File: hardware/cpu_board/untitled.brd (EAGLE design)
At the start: 126.3 x 94.6 mm, 83 parts, among them IC1 MAX232ECWE, IC2 MAX232ECWE, IC3 AM29F040J, IC4 74HCT138D, IC5 LM2596S, IC6 74HCT273DW, IC7 74LVC1G08DBV, IC8 74LVC1G04DBV, IC9 74HCT138D, J2 POWER_JACKSLT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

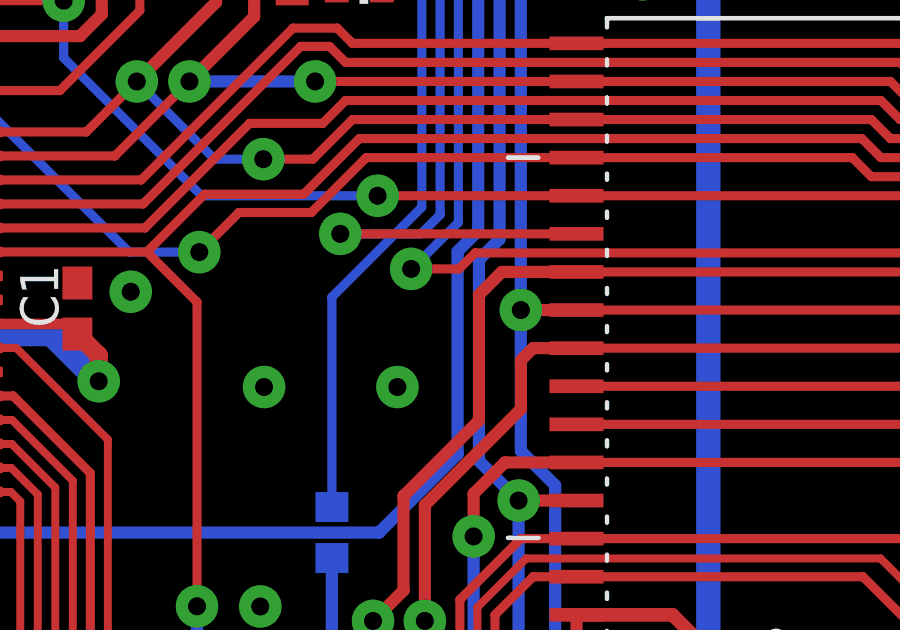
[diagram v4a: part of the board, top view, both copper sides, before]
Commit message: Mionor bug fixed
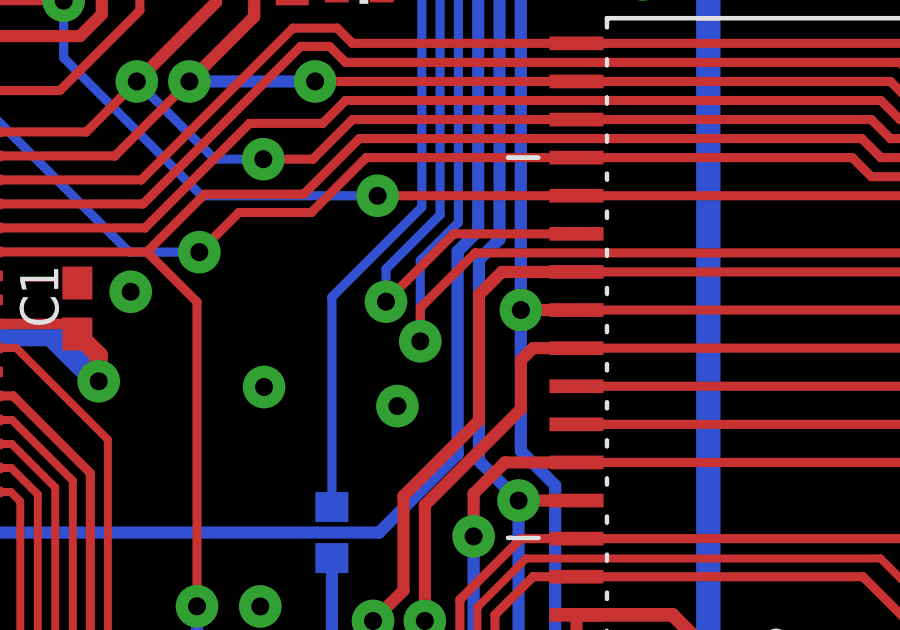
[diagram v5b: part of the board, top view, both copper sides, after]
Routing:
- net !ROM_CS: track 59.5 -> 63.2 mm
- net !RAM_CS: track 52.1 -> 51.6 mm
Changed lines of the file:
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@@
 <contactref element="IC9" pad="1"/>
 <contactref element="IC9" pad="5"/>
-<via x="67.7418" y="34.8234" extent="1-16" drill="0.6" diameter="1.4224" shape="octagon"/>
+<via x="67.7418" y="34.1884" extent="1-16" drill="0.6" diameter="1.4224" shape="octagon"/>
 <wire x1="4.064" y1="-9.359" x2="16.6624" y2="-7.9398" width="0" layer="19" extent="1-1"/>
 <wire x1="14.605" y1="7.62" x2="16.6624" y2="-7.9398" width="0" layer="19" extent="1-1"/>
@@
 <contactref element="IC3" pad="22"/>
 <wire x1="95.6206" y1="39.2938" x2="70.3326" y2="39.2938" width="0.3048" layer="1"/>
-<via x="68.199" y="38.7604" extent="1-16" drill="0.6" diameter="1.4224" shape="octagon"/>
-<wire x1="68.199" y1="38.7604" x2="69.7992" y2="38.7604" width="0.3048" layer="1"/>
-<wire x1="69.7992" y1="38.7604" x2="70.3326" y2="39.2938" width="0.3048" layer="1"/>
+<via x="68.5038" y="36.3474" extent="1-16" drill="0.6" diameter="1.4224" shape="octagon"/>
 <wire x1="65.4304" y1="54.864" x2="65.4304" y2="61.1886" width="0.3048" layer="16"/>
 <contactref element="IC9" pad="15"/>
-<wire x1="68.199" y1="38.7604" x2="68.2244" y2="38.7604" width="0.3048" layer="16"/>
-<wire x1="68.2244" y1="38.7604" x2="69.7738" y2="40.3098" width="0.3048" layer="16"/>
+<wire x1="68.5038" y1="39.0398" x2="69.7738" y2="40.3098" width="0.3048" layer="16"/>
 <wire x1="69.7738" y1="40.3098" x2="69.7738" y2="50.5206" width="0.3048" layer="16"/>
 <wire x1="61.6966" y1="66.6496" x2="61.6966" y2="64.9224" width="0.3048" layer="16"/>
 <wire x1="61.6966" y1="64.9224" x2="65.4304" y2="61.1886" width="0.3048" layer="16"/>
 <wire x1="69.7738" y1="50.5206" x2="65.4304" y2="54.864" width="0.3048" layer="16"/>
+<wire x1="68.5038" y1="36.3474" x2="68.5038" y2="39.0398" width="0.3048" layer="16"/>
+<wire x1="68.5038" y1="36.3474" x2="68.5038" y2="37.465" width="0.3048" layer="1"/>
+<wire x1="68.5038" y1="37.465" x2="70.3326" y2="39.2938" width="0.3048" layer="1"/>
 </signal>
 <signal name="!RAM_CS">
 <contactref element="U1" pad="22"/>
-<via x="65.8368" y="39.9288" extent="1-16" drill="0.6" diameter="1.4224" shape="octagon"/>
-<wire x1="73.7108" y1="39.9288" x2="65.8368" y2="39.9288" width="0.3048" layer="1"/>
+<via x="67.3608" y="37.6682" extent="1-16" drill="0.6" diameter="1.4224" shape="octagon"/>
 <wire x1="64.8208" y1="54.61" x2="64.8208" y2="60.9346" width="0.3048" layer="16"/>
-<wire x1="65.8368" y1="39.9288" x2="68.5292" y2="39.9288" width="0.3048" layer="16"/>
-<wire x1="68.5292" y1="39.9288" x2="69.1642" y2="40.5638" width="0.3048" layer="16"/>
 <wire x1="69.1642" y1="40.5638" x2="69.1642" y2="50.2666" width="0.3048" layer="16"/>
 <wire x1="64.8208" y1="60.9346" x2="61.0616" y2="64.6938" width="0.3048" layer="16"/>
@@
 <wire x1="61.0616" y1="71.1904" x2="61.2022" y2="71.331" width="0.3048" layer="16"/>
 <wire x1="69.1642" y1="50.2666" x2="64.8208" y2="54.61" width="0.3048" layer="16"/>
+<wire x1="67.3608" y1="37.6682" x2="67.3608" y2="38.7604" width="0.3048" layer="16"/>
+<wire x1="67.3608" y1="38.7604" x2="69.1642" y2="40.5638" width="0.3048" layer="16"/>
+<wire x1="73.7108" y1="39.9288" x2="69.6214" y2="39.9288" width="0.3048" layer="1"/>
+<wire x1="69.6214" y1="39.9288" x2="67.3608" y2="37.6682" width="0.3048" layer="1"/>
 </signal>
 <signal name="N$25">
@@
 <contactref element="IC9" pad="3"/>
 <wire x1="65.5574" y1="30.822" x2="65.5574" y2="37.8206" width="0.3048" layer="16"/>
-<wire x1="65.5574" y1="37.8206" x2="68.5546" y2="40.8178" width="0.3048" layer="16"/>
 <wire x1="68.5546" y1="40.8178" x2="68.5546" y2="50.0126" width="0.3048" layer="16"/>
 <wire x1="60.4266" y1="58.1406" x2="60.4266" y2="60.5028" width="0.3048" layer="16"/>
 <wire x1="68.5546" y1="50.0126" x2="60.4266" y2="58.1406" width="0.3048" layer="16"/>
+<wire x1="68.5546" y1="40.8178" x2="65.5574" y2="37.8206" width="0.3048" layer="16"/>
 </signal>
 <signal name="N$44">

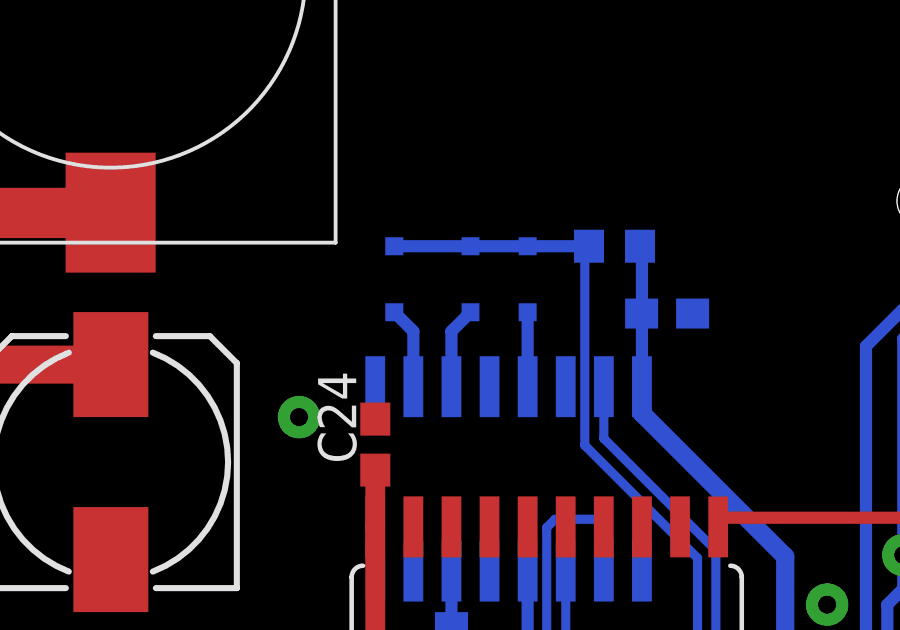
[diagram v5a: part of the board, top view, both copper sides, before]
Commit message: ROM/RAM address decoder bug fix
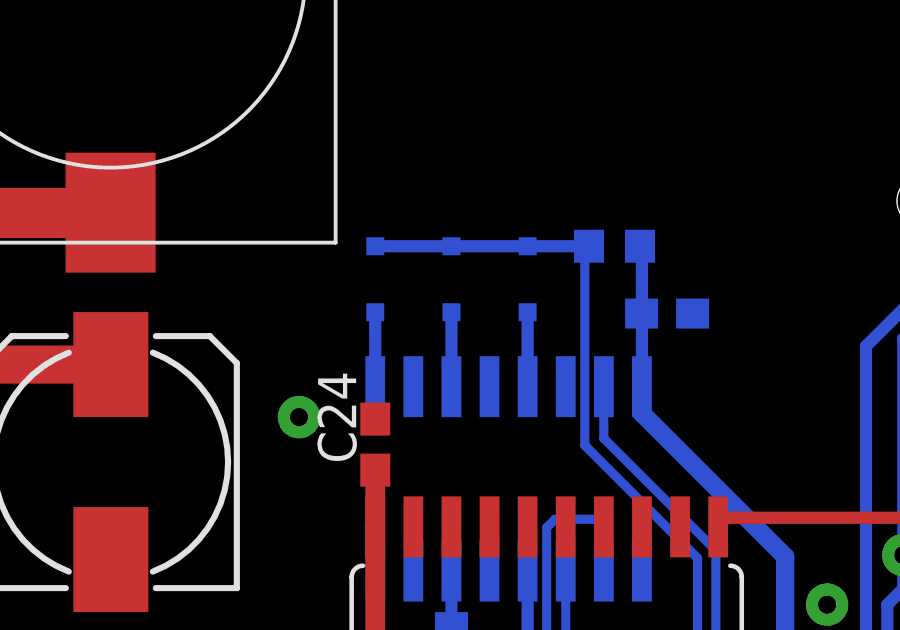
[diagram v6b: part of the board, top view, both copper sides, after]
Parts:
- moved D3 0.64 mm to (56.6, 70.2)
- moved D4 0.63 mm to (54.1, 70.2)
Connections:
- net N$50: now also IC9.9; no longer IC9.10
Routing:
- net !RAM_CS: track 51.6 -> 52.2 mm
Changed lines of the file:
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@@
 <element name="R18" library="rcl" package="R0603" value="" x="56.6166" y="57.785" rot="MR270"/>
 <element name="D2" library="adafruit" package="SOD-323" value="" x="59.1566" y="70.231" rot="MR90"/>
-<element name="D3" library="adafruit" package="SOD-323" value="" x="57.2516" y="70.231" rot="MR90"/>
-<element name="D4" library="adafruit" package="SOD-323" value="" x="54.7116" y="70.231" rot="MR90"/>
+<element name="D3" library="adafruit" package="SOD-323" value="" x="56.6166" y="70.231" rot="MR90"/>
+<element name="D4" library="adafruit" package="SOD-323" value="" x="54.0766" y="70.231" rot="MR90"/>
 <element name="R19" library="rcl" package="R0603" value="" x="62.0522" y="71.331" rot="MR180"/>
 </elements>
@@
 <contactref element="D4" pad="A"/>
 <contactref element="D3" pad="A"/>
-<wire x1="54.7116" y1="71.331" x2="57.2516" y2="71.331" width="0.4064" layer="16"/>
-<wire x1="57.2516" y1="71.331" x2="59.1566" y2="71.331" width="0.4064" layer="16"/>
+<wire x1="54.0766" y1="71.331" x2="56.6166" y2="71.331" width="0.4064" layer="16"/>
+<wire x1="56.6166" y1="71.331" x2="59.1566" y2="71.331" width="0.4064" layer="16"/>
 <wire x1="59.1566" y1="71.331" x2="61.2022" y2="71.331" width="0.4064" layer="16"/>
 <contactref element="R19" pad="1"/>
@@
 </signal>
 <signal name="N$50">
-<contactref element="IC9" pad="10"/>
 <contactref element="D4" pad="C"/>
-<wire x1="55.3466" y1="66.6496" x2="55.3466" y2="68.496" width="0.4064" layer="16"/>
-<wire x1="55.3466" y1="68.496" x2="54.7116" y2="69.131" width="0.4064" layer="16"/>
+<contactref element="IC9" pad="9"/>
+<wire x1="54.0766" y1="66.6496" x2="54.0766" y2="69.131" width="0.4064" layer="16"/>
 </signal>
 <signal name="N$51">
 <contactref element="IC9" pad="11"/>
 <contactref element="D3" pad="C"/>
-<wire x1="56.6166" y1="66.6496" x2="56.6166" y2="68.496" width="0.4064" layer="16"/>
-<wire x1="56.6166" y1="68.496" x2="57.2516" y2="69.131" width="0.4064" layer="16"/>
+<wire x1="56.6166" y1="66.6496" x2="56.6166" y2="69.131" width="0.4064" layer="16"/>
 </signal>
 </signals>

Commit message: Capacitor added
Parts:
- removed C15: (no value), rcl:C0603
- C3: device rcl:C0402 -> rcl:C0603
- moved C3 40.7 mm to (24.1, 32.7)
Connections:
- net 5V: no longer C15.1
- net GND: no longer C15.2
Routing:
- net 5V: track 514.9 -> 515.0 mm, vias 15 -> 14
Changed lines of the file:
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@@
 <element name="C1" library="rcl" package="C0603" value="" x="57.0738" y="37.4396" rot="R90"/>
 <element name="C2" library="rcl" package="C0603" value="" x="63.8048" y="69.088" rot="MR180"/>
-<element name="C3" library="rcl" package="C0402" value="" x="16.6624" y="-7.2898" rot="R270"/>
 <element name="X1" library="con-subd" package="M09HP" value="" x="11.43" y="25.4" rot="R270">
 <attribute name="OC_NEWARK" value="unknown" x="0" y="25.4" size="1.778" layer="27" rot="R270" display="off"/>
@@
 <element name="JP10" library="pinhead" package="1X08" value="" x="45.72" y="9.6266" rot="R180"/>
 <element name="JP11" library="pinhead" package="1X18" value="" x="83.82" y="9.6266" rot="R180"/>
-<element name="C15" library="rcl" package="C0603" value="" x="4.064" y="-8.509" rot="R270"/>
 <element name="U$4" library="mw" package="QFP80" value="HD64180" x="42.2402" y="36.8554"/>
 <element name="U$3" library="crystal" package="ASE" value="ASE" x="27.5082" y="34.4678">
@@
 <element name="D4" library="adafruit" package="SOD-323" value="" x="54.0766" y="70.231" rot="MR90"/>
 <element name="R19" library="rcl" package="R0603" value="" x="62.0522" y="71.331" rot="MR180"/>
+<element name="C3" library="rcl" package="C0603" value="" x="24.13" y="32.7152" rot="R270"/>
 </elements>
 <signals>
@@
 <vertex x="126.365" y="94.615"/>
 </polygon>
-<contactref element="C3" pad="2"/>
 <contactref element="C2" pad="2"/>
 <contactref element="C1" pad="2"/>
@@
 <contactref element="C31" pad="-"/>
 <via x="58.42" y="9.525" extent="1-16" drill="0.6" diameter="1.4224" shape="octagon"/>
-<contactref element="C15" pad="2"/>
 <contactref element="U$4" pad="12"/>
 <contactref element="U$4" pad="34"/>
@@
 <contactref element="IC9" pad="5"/>
 <via x="67.7418" y="34.1884" extent="1-16" drill="0.6" diameter="1.4224" shape="octagon"/>
-<wire x1="4.064" y1="-9.359" x2="16.6624" y2="-7.9398" width="0" layer="19" extent="1-1"/>
-<wire x1="14.605" y1="7.62" x2="16.6624" y2="-7.9398" width="0" layer="19" extent="1-1"/>
+<contactref element="C3" pad="2"/>
 </signal>
 <signal name="5V">
@@
 <contactref element="IC1" pad="16"/>
 <contactref element="C1" pad="1"/>
-<contactref element="C3" pad="1"/>
 <contactref element="C2" pad="1"/>
 <contactref element="C9" pad="2"/>
@@
 <wire x1="93.36" y1="59.1044" x2="93.345" y2="59.1194" width="0.6096" layer="1"/>
 <contactref element="C31" pad="+"/>
-<via x="4.064" y="-6.0979" extent="1-16" drill="0.6" diameter="1.4224" shape="octagon"/>
-<contactref element="C15" pad="1"/>
-<wire x1="4.064" y1="-7.659" x2="4.064" y2="-6.0979" width="0.6096" layer="1"/>
 <contactref element="U$4" pad="32"/>
 <via x="34.6456" y="26.8986" extent="1-16" drill="0.6" diameter="1.4224" shape="octagon"/>
@@
 <wire x1="68.1944" y1="56.9514" x2="67.7464" y2="56.9514" width="0.8128" layer="1"/>
 <wire x1="67.7464" y1="56.9514" x2="67.7418" y2="56.9468" width="0.8128" layer="1"/>
-<wire x1="16.6624" y1="-6.6398" x2="31.75" y2="12.7" width="0" layer="19" extent="1-16"/>
-<wire x1="4.064" y1="-6.0979" x2="16.6624" y2="-6.6398" width="0" layer="19" extent="1-1"/>
+<contactref element="C3" pad="1"/>
+<wire x1="24.13" y1="35.2928" x2="24.13" y2="33.5652" width="0.6096" layer="1"/>
 </signal>
 <signal name="N$7">

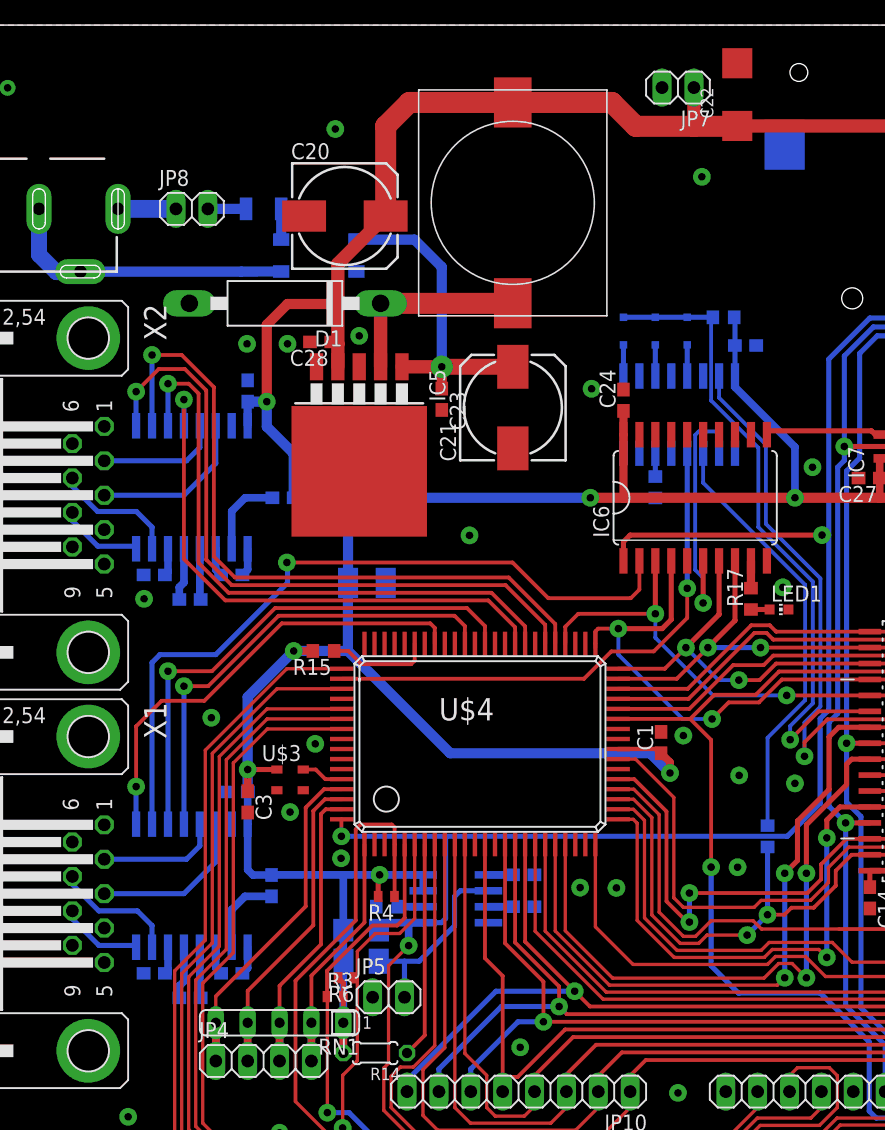
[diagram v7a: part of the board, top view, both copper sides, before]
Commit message: CPU size fixed
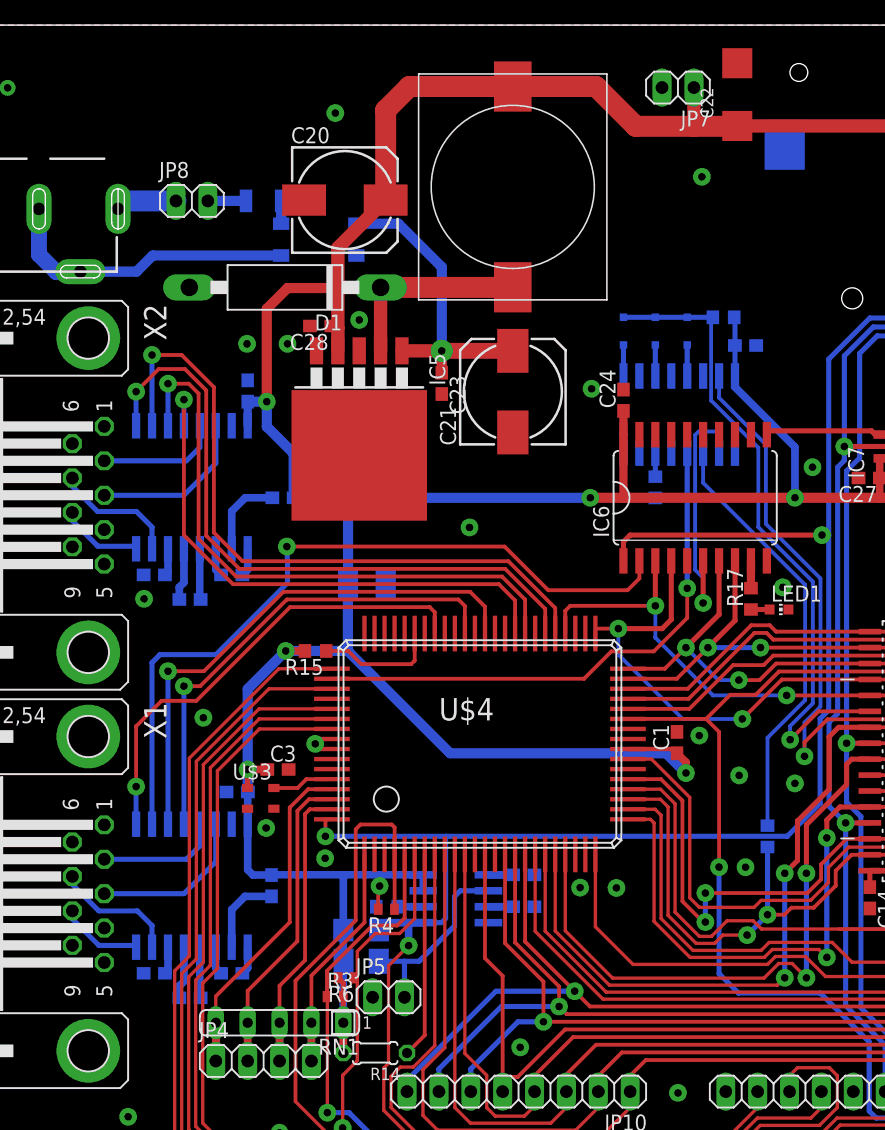
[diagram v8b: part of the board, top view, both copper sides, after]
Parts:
- U$4: value HD64180 -> HD64180QFP80_
- moved C3 3.53 mm to (26.5, 35.3), turned to 0 degrees
- moved U$3 2.76 mm to (25.2, 33.0)
- moved D1 1.27 mm to (27.1, 73.7)
- moved L2 1.27 mm to (52.8, 72.7)
- moved C1 1.27 mm to (58.3, 37.4)
- moved IC5 1.27 mm to (33.0, 62.9)
- moved B1 1.27 mm to (29.8, 77.5)
- moved C20 1.27 mm to (31.9, 80.7)
- moved C21 1.27 mm to (45.3, 65.4)
- moved C23 1.27 mm to (39.6, 66.1)
- moved C28 1.27 mm to (29.9, 70.6)
- moved R4 1.02 mm to (35.2, 24.2)
- moved F1 0.64 mm to (25.4, 80.6)
- moved JP8 0.64 mm to (19.7, 80.6)
- moved R15 0.64 mm to (29.5, 44.7)
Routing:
- net 5V: track 515.0 -> 519.0 mm
- net !RST: track 186.1 -> 187.8 mm
- net EXTAL: track 3.40 -> 4.92 mm
- net N$25: track 8.32 -> 9.76 mm
- net D0: track 146.0 -> 144.7 mm
- net RXD2: track 37.5 -> 38.7 mm
- net TXD2: track 41.5 -> 42.7 mm
- net CTS1: track 53.9 -> 52.7 mm
- net RTS1: track 56.1 -> 54.9 mm
- net !INT: track 78.8 -> 79.8 mm
- net CTS2: track 36.4 -> 37.4 mm
- net A9: track 120.1 -> 119.3 mm
- net A7: track 126.5 -> 125.7 mm
- net A3: track 136.6 -> 135.8 mm
- net A11: track 71.2 -> 70.4 mm
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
